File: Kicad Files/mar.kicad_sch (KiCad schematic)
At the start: 21 parts

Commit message: started tidy up in control
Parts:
- gave numbers to parts that had none: 21
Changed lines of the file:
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@@
   (symbol (lib_id "8bit-computer-rescue:LED_ALT-Device") (at 160.02 30.48 180) (unit 1)
     (in_bom yes) (on_board yes)
-    (property "Reference" "" (id 0) (at 160.02 33.02 0))
+    (property "Reference" "D96" (id 0) (at 160.02 33.02 0))
     (property "Value" "YELLOW" (id 1) (at 160.02 27.94 0))
     (property "Footprint" "LED_THT:LED_D5.0mm" (id 2) (at 160.02 30.48 0)
@@
   (symbol (lib_id "8bit-computer-rescue:LED_ALT-Device") (at 160.02 38.1 180) (unit 1)
     (in_bom yes) (on_board yes)
-    (property "Reference" "" (id 0) (at 160.02 40.64 0))
+    (property "Reference" "D97" (id 0) (at 160.02 40.64 0))
     (property "Value" "YELLOW" (id 1) (at 160.02 35.56 0))
     (property "Footprint" "LED_THT:LED_D5.0mm" (id 2) (at 160.02 38.1 0)
@@
   (symbol (lib_id "8bit-computer-rescue:LED_ALT-Device") (at 160.02 45.72 180) (unit 1)
     (in_bom yes) (on_board yes)
-    (property "Reference" "" (id 0) (at 160.02 48.26 0))
+    (property "Reference" "D98" (id 0) (at 160.02 48.26 0))
     (property "Value" "YELLOW" (id 1) (at 160.02 43.18 0))
     (property "Footprint" "LED_THT:LED_D5.0mm" (id 2) (at 160.02 45.72 0)
@@
   (symbol (lib_id "8bit-computer-rescue:LED_ALT-Device") (at 160.02 53.34 180) (unit 1)
     (in_bom yes) (on_board yes)
-    (property "Reference" "" (id 0) (at 160.02 55.88 0))
+    (property "Reference" "D99" (id 0) (at 160.02 55.88 0))
     (property "Value" "YELLOW" (id 1) (at 160.02 50.8 0))
     (property "Footprint" "LED_THT:LED_D5.0mm" (id 2) (at 160.02 53.34 0)
@@
   (symbol (lib_id "Device:R") (at 170.18 30.48 90) (unit 1)
     (in_bom yes) (on_board yes)
-    (property "Reference" "" (id 0) (at 170.18 28.448 90))
+    (property "Reference" "R126" (id 0) (at 170.18 28.448 90))
     (property "Value" "220" (id 1) (at 170.18 30.48 90))
     (property "Footprint" "Resistor_THT:R_Axial_DIN0207_L6.3mm_D2.5mm_P7.62mm_Horizontal" (id 2) (at 170.18 32.258 90)
@@
   (symbol (lib_id "Device:R") (at 170.18 38.1 90) (unit 1)
     (in_bom yes) (on_board yes)
-    (property "Reference" "" (id 0) (at 170.18 36.068 90))
+    (property "Reference" "R127" (id 0) (at 170.18 36.068 90))
     (property "Value" "220" (id 1) (at 170.18 38.1 90))
     (property "Footprint" "Resistor_THT:R_Axial_DIN0207_L6.3mm_D2.5mm_P7.62mm_Horizontal" (id 2) (at 170.18 39.878 90)
@@
   (symbol (lib_id "Device:R") (at 170.18 45.72 90) (unit 1)
     (in_bom yes) (on_board yes)
-    (property "Reference" "" (id 0) (at 170.18 43.688 90))
+    (property "Reference" "R128" (id 0) (at 170.18 43.688 90))
     (property "Value" "220" (id 1) (at 170.18 45.72 90))
     (property "Footprint" "Resistor_THT:R_Axial_DIN0207_L6.3mm_D2.5mm_P7.62mm_Horizontal" (id 2) (at 170.18 47.498 90)
@@
   (symbol (lib_id "Device:R") (at 170.18 53.34 90) (unit 1)
     (in_bom yes) (on_board yes)
-    (property "Reference" "" (id 0) (at 170.18 51.308 90))
+    (property "Reference" "R129" (id 0) (at 170.18 51.308 90))
     (property "Value" "220" (id 1) (at 170.18 53.34 90))
     (property "Footprint" "Resistor_THT:R_Axial_DIN0207_L6.3mm_D2.5mm_P7.62mm_Horizontal" (id 2) (at 170.18 55.118 90)
@@
   (symbol (lib_id "Device:C") (at 171.45 140.97 0) (unit 1)
     (in_bom yes) (on_board yes)
-    (property "Reference" "" (id 0) (at 172.085 138.43 0)
+    (property "Reference" "C16" (id 0) (at 172.085 138.43 0)
       (effects (font (size 1.27 1.27)) (justify left))
     )
@@
   (symbol (lib_id "74xx:74LS157") (at 144.78 107.95 90) (unit 1)
     (in_bom yes) (on_board yes)
-    (property "Reference" "" (id 0) (at 171.2976 106.7816 90)
+    (property "Reference" "U57" (id 0) (at 171.2976 106.7816 90)
       (effects (font (size 1.27 1.27)) (justify right))
     )
@@
   (symbol (lib_id "74xx:74LS157") (at 68.58 107.95 90) (unit 1)
     (in_bom yes) (on_board yes)
-    (property "Reference" "" (id 0) (at 95.0976 106.7816 90)
+    (property "Reference" "U56" (id 0) (at 95.0976 106.7816 90)
       (effects (font (size 1.27 1.27)) (justify right))
     )
@@
   (symbol (lib_id "74xx:74LS173") (at 144.78 168.91 90) (unit 1)
     (in_bom yes) (on_board yes)
-    (property "Reference" "" (id 0) (at 168.7576 167.7416 90)
+    (property "Reference" "U59" (id 0) (at 168.7576 167.7416 90)
       (effects (font (size 1.27 1.27)) (justify right))
     )
@@
   (symbol (lib_id "74xx:74LS173") (at 68.58 168.91 90) (unit 1)
     (in_bom yes) (on_board yes)
-    (property "Reference" "" (id 0) (at 92.5576 167.7416 90)
+    (property "Reference" "U58" (id 0) (at 92.5576 167.7416 90)
       (effects (font (size 1.27 1.27)) (justify right))
     )
@@
   (symbol (lib_id "8bit-computer-rescue:LED_ALT-Device") (at 160.02 60.96 180) (unit 1)
     (in_bom yes) (on_board yes)
-    (property "Reference" "" (id 0) (at 160.02 63.5 0))
+    (property "Reference" "D100" (id 0) (at 160.02 63.5 0))
     (property "Value" "YELLOW" (id 1) (at 160.02 58.42 0))
     (property "Footprint" "LED_THT:LED_D5.0mm" (id 2) (at 160.02 60.96 0)
@@
   (symbol (lib_id "8bit-computer-rescue:LED_ALT-Device") (at 160.02 68.58 180) (unit 1)
     (in_bom yes) (on_board yes)
-    (property "Reference" "" (id 0) (at 160.02 71.12 0))
+    (property "Reference" "D101" (id 0) (at 160.02 71.12 0))
     (property "Value" "YELLOW" (id 1) (at 160.02 66.04 0))
     (property "Footprint" "LED_THT:LED_D5.0mm" (id 2) (at 160.02 68.58 0)
@@
   (symbol (lib_id "8bit-computer-rescue:LED_ALT-Device") (at 160.02 76.2 180) (unit 1)
     (in_bom yes) (on_board yes)
-    (property "Reference" "" (id 0) (at 160.02 78.74 0))
+    (property "Reference" "D102" (id 0) (at 160.02 78.74 0))
     (property "Value" "YELLOW" (id 1) (at 160.02 73.66 0))
     (property "Footprint" "LED_THT:LED_D5.0mm" (id 2) (at 160.02 76.2 0)
@@
   (symbol (lib_id "8bit-computer-rescue:LED_ALT-Device") (at 160.02 83.82 180) (unit 1)
     (in_bom yes) (on_board yes)
-    (property "Reference" "" (id 0) (at 160.02 86.36 0))
+    (property "Reference" "D103" (id 0) (at 160.02 86.36 0))
     (property "Value" "YELLOW" (id 1) (at 160.02 81.28 0))
     (property "Footprint" "LED_THT:LED_D5.0mm" (id 2) (at 160.02 83.82 0)
@@
   (symbol (lib_id "Device:R") (at 170.18 60.96 90) (unit 1)
     (in_bom yes) (on_board yes)
-    (property "Reference" "" (id 0) (at 170.18 58.928 90))
+    (property "Reference" "R130" (id 0) (at 170.18 58.928 90))
     (property "Value" "220" (id 1) (at 170.18 60.96 90))
     (property "Footprint" "Resistor_THT:R_Axial_DIN0207_L6.3mm_D2.5mm_P7.62mm_Horizontal" (id 2) (at 170.18 62.738 90)
@@
   (symbol (lib_id "Device:R") (at 170.18 68.58 90) (unit 1)
     (in_bom yes) (on_board yes)
-    (property "Reference" "" (id 0) (at 170.18 66.548 90))
+    (property "Reference" "R131" (id 0) (at 170.18 66.548 90))
     (property "Value" "220" (id 1) (at 170.18 68.58 90))
     (property "Footprint" "Resistor_THT:R_Axial_DIN0207_L6.3mm_D2.5mm_P7.62mm_Horizontal" (id 2) (at 170.18 70.358 90)
@@
   (symbol (lib_id "Device:R") (at 170.18 76.2 90) (unit 1)
     (in_bom yes) (on_board yes)
-    (property "Reference" "" (id 0) (at 170.18 74.168 90))
+    (property "Reference" "R132" (id 0) (at 170.18 74.168 90))
     (property "Value" "220" (id 1) (at 170.18 76.2 90))
     (property "Footprint" "Resistor_THT:R_Axial_DIN0207_L6.3mm_D2.5mm_P7.62mm_Horizontal" (id 2) (at 170.18 77.978 90)
@@
   (symbol (lib_id "Device:R") (at 170.18 83.82 90) (unit 1)
     (in_bom yes) (on_board yes)
-    (property "Reference" "" (id 0) (at 170.18 81.788 90))
+    (property "Reference" "R133" (id 0) (at 170.18 81.788 90))
     (property "Value" "220" (id 1) (at 170.18 83.82 90))
     (property "Footprint" "Resistor_THT:R_Axial_DIN0207_L6.3mm_D2.5mm_P7.62mm_Horizontal" (id 2) (at 170.18 85.598 90)

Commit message: work on cl
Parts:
- C10: renamed from C16; value 0.1µF -> C
- R46: renamed from R126; value 220 -> R
- R47: renamed from R127; value 220 -> R
- R48: renamed from R128; value 220 -> R
- R49: renamed from R129; value 220 -> R
- R50: renamed from R130; value 220 -> R
- R51: renamed from R131; value 220 -> R
- R52: renamed from R132; value 220 -> R
- R53: renamed from R133; value 220 -> R
- renumbered D96 to D16, D97 to D17, D98 to D18, D99 to D19, D100 to D20, D101 to D21, D102 to D22, D103 to D23, U56 to U13, U58 to U14, U57 to U15, U59 to U16

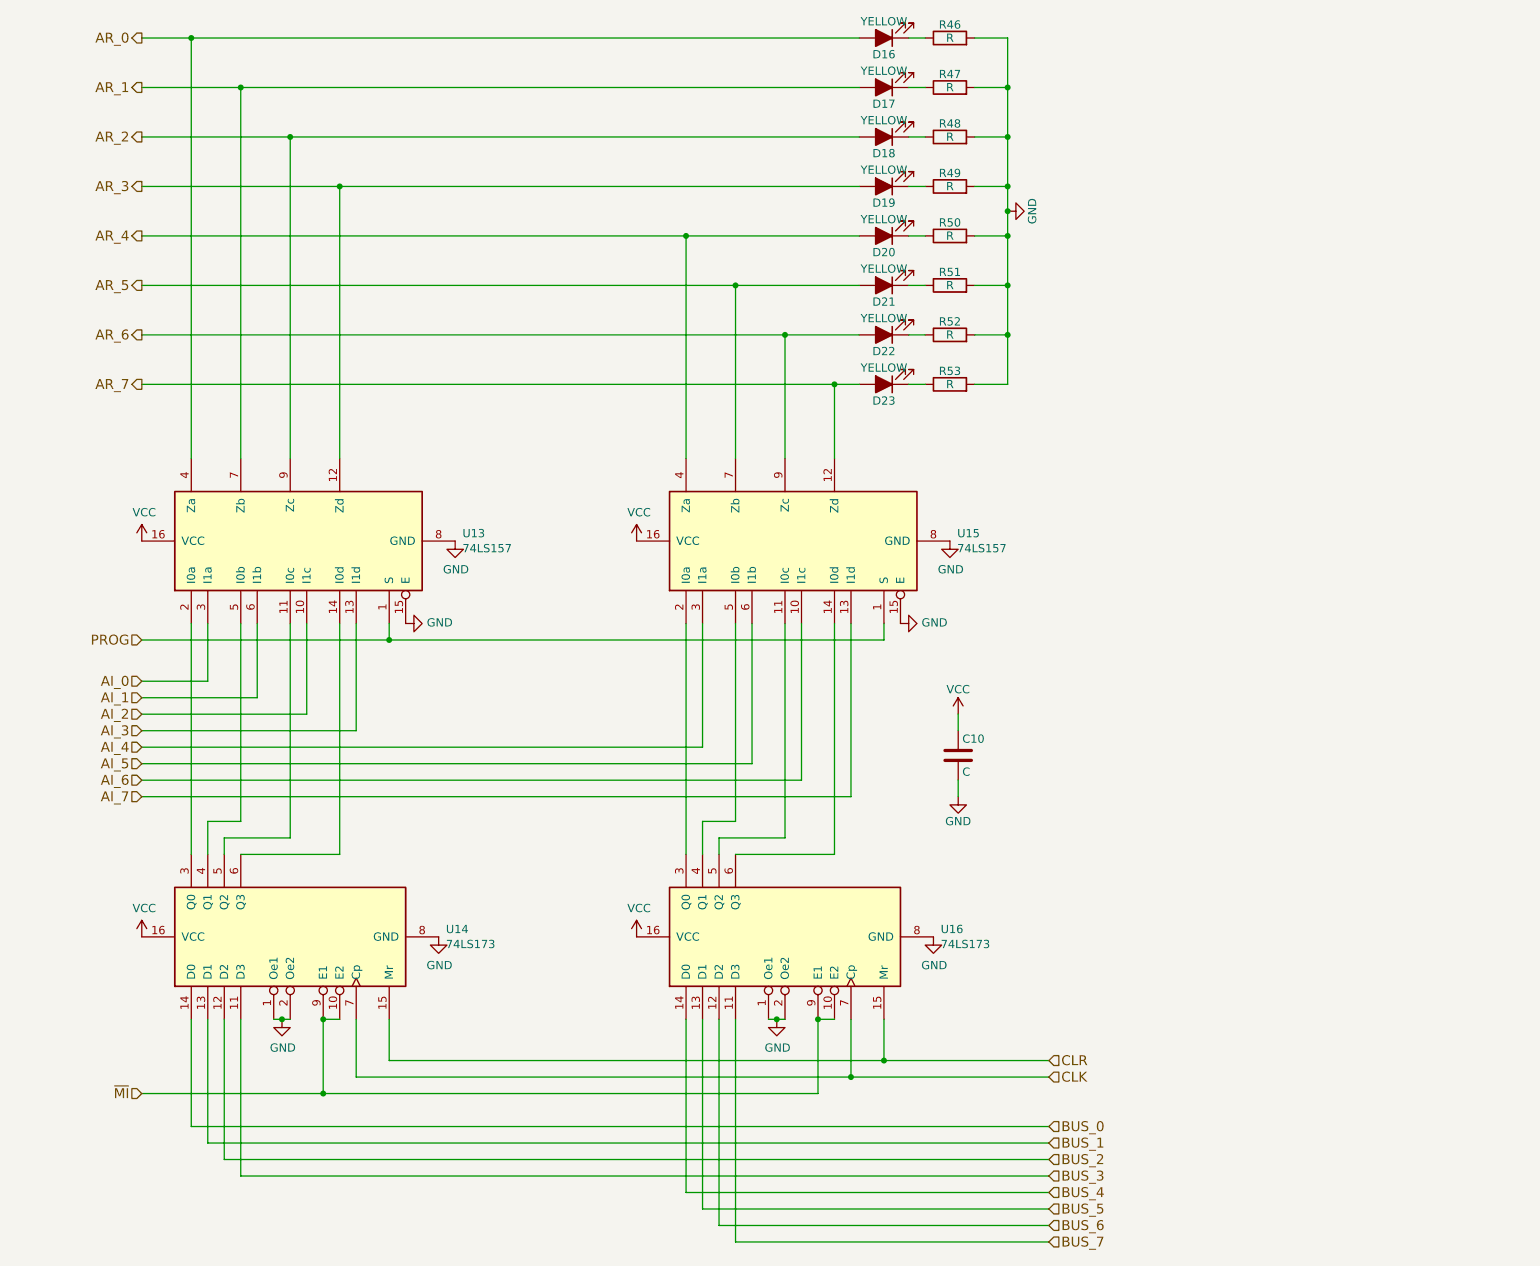
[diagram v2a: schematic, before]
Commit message: changed to 16bit Addr Bus
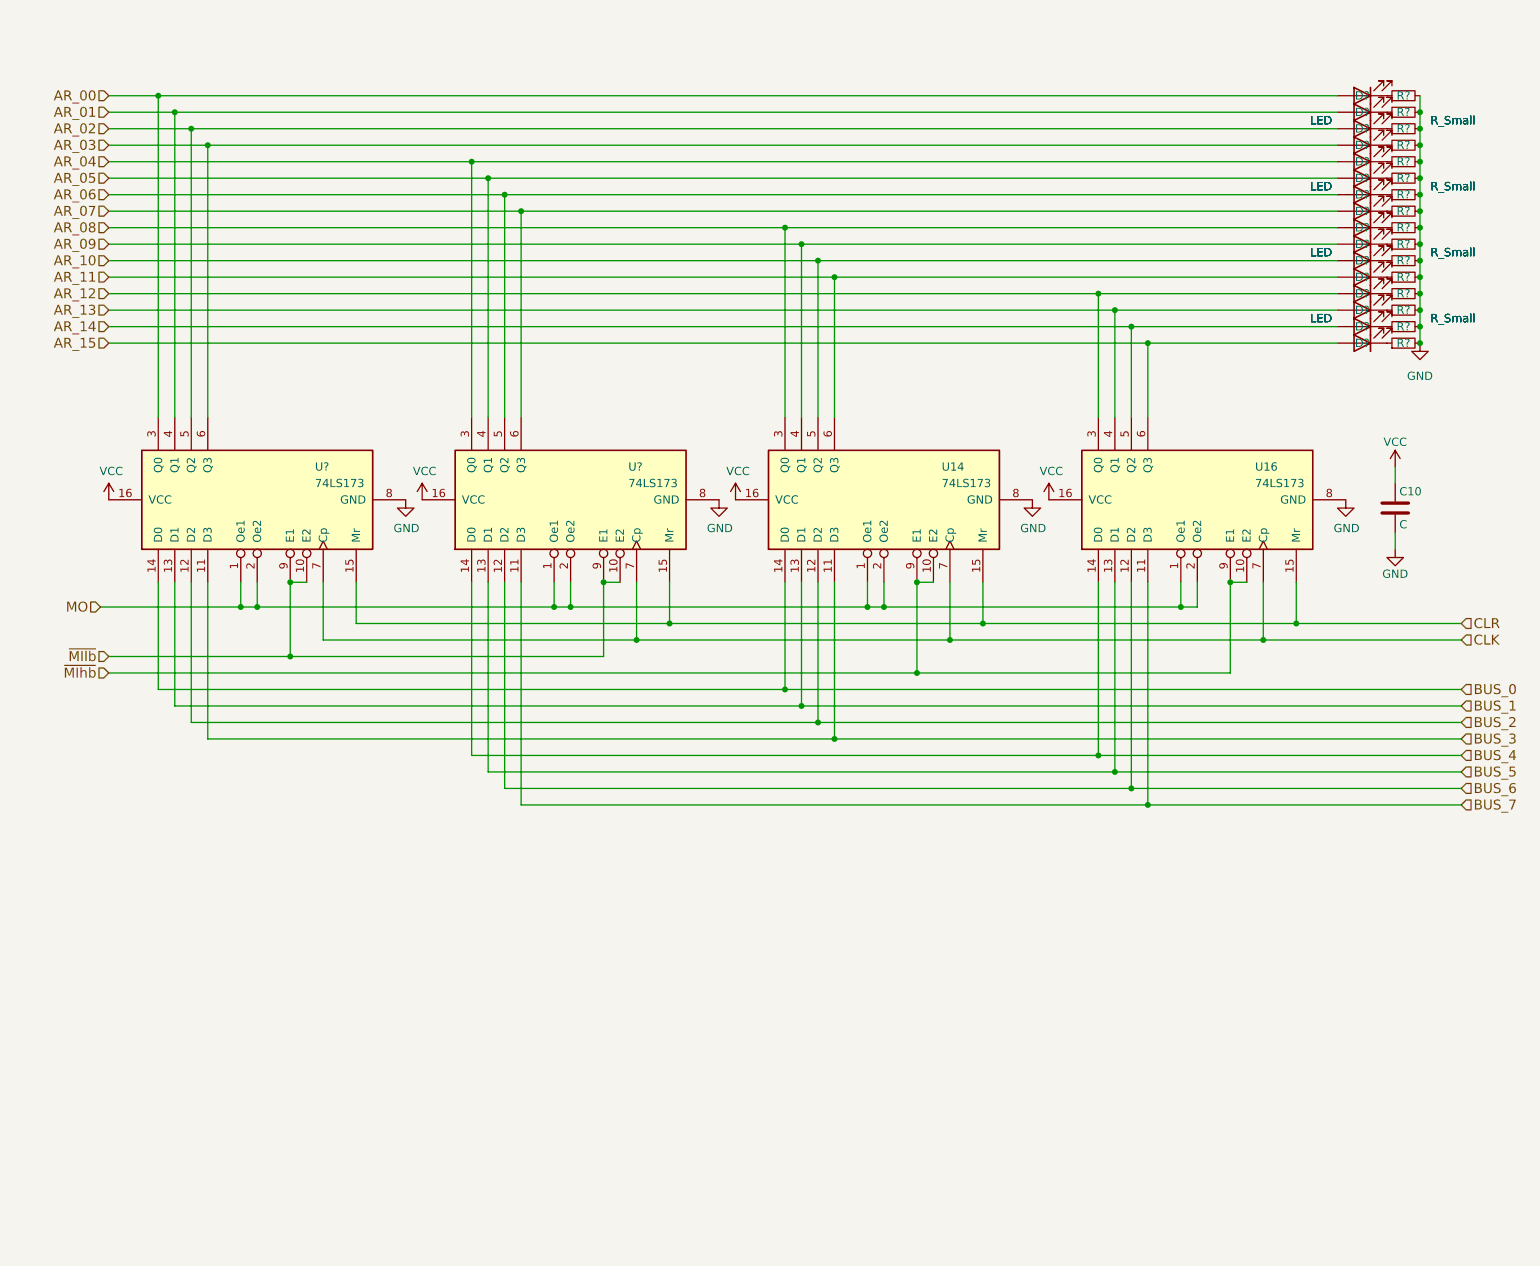
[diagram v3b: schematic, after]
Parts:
- removed D16, D17, D18, D19, D20, D21, D22, D23: YELLOW, LED_THT:LED_D5.0mm, symbol 8bit-computer-rescue:LED_ALT-Device
- removed R46, R47, R48, R49, R50, R51, R52, R53: R, Resistor_THT:R_Axial_DIN0207_L6.3mm_D2.5mm_P7.62mm_Horizontal, symbol Device:R
- removed U13, U15: 74LS157, symbol 74xx:74LS157
- added D? (x16): LED, symbol Device:LED
- added R? (x16): R_Small, symbol Device:R_Small
- added U? (x2): 74LS173, symbol 74xx:74LS173
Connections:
- net BUS_0: now also U?.14 (D0)
- net BUS_1: now also U?.13 (D1)
- net BUS_2: now also U?.12 (D2)
- net BUS_3: now also U?.11 (D3)
- net BUS_4: now also U?.14 (D0)
- net BUS_5: now also U?.13 (D1)
- net BUS_6: now also U?.12 (D2)
- net BUS_7: now also U?.11 (D3)
- net CLK: now also U?.7 (Cp), U?.7 (Cp)
- net CLR: now also U?.15 (Mr), U?.15 (Mr)
- net GND: now also R?.2, R?.2, R?.2, R?.2, R?.2, R?.2, R?.2, R?.2, R?.2, R?.2, R?.2, R?.2, R?.2, R?.2, R?.2, R?.2, U?.8 (GND), U?.8 (GND); no longer U14.1 (Oe1), U14.2 (Oe2), U16.1 (Oe1), U16.2 (Oe2)
- net VCC: now also U?.16 (VCC), U?.16 (VCC)
- net AR_14: now reaches U16.5 (Q2)
- net AR_14: now also D?.2 (A)
- net AR_15: now reaches U16.6 (Q3)
- net AR_15: now also D?.2 (A)
- net AR_12: now reaches U16.3 (Q0)
- net AR_12: now also D?.2 (A)
- net AR_13: now reaches U16.4 (Q1)
- net AR_13: now also D?.2 (A)
- net AR_10: now reaches U14.5 (Q2)
- net AR_10: now also D?.2 (A)
- net AR_11: now reaches U14.6 (Q3)
- net AR_11: now also D?.2 (A)
- net AR_08: now reaches U14.3 (Q0)
- net AR_08: now also D?.2 (A)
- net AR_09: now reaches U14.4 (Q1)
- net AR_09: now also D?.2 (A)
- net ~{MI} renamed ~{MIhb}
- new net: D?.1 (K), R?.1 (x16)
- new net AR_00: D?.2 (A), U?.3 (Q0)
- new net AR_01: D?.2 (A), U?.4 (Q1)
- new net AR_02: D?.2 (A), U?.5 (Q2)
- new net AR_03: D?.2 (A), U?.6 (Q3)
- new net AR_04: D?.2 (A), U?.3 (Q0)
- new net AR_05: D?.2 (A), U?.4 (Q1)
- new net AR_06: D?.2 (A), U?.5 (Q2)
- new net AR_07: D?.2 (A), U?.6 (Q3)
- new net MO: U14.1 (Oe1), U14.2 (Oe2), U16.1 (Oe1), U16.2 (Oe2), U?.1 (Oe1), U?.1 (Oe1), U?.2 (Oe2), U?.2 (Oe2)
- new net ~{MIlb}: U?.10 (E2), U?.10 (E2), U?.9 (E1), U?.9 (E1)
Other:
- moved on the sheet: C10, U14, U16

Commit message: w1
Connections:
- net AR_00 renamed ABUS_00
- net AR_01 renamed ABUS_01
- net AR_02 renamed ABUS_02
- net AR_03 renamed ABUS_03
- net AR_04 renamed ABUS_04
- net AR_05 renamed ABUS_05
- net AR_06 renamed ABUS_06
- net AR_07 renamed ABUS_07
- net AR_08 renamed ABUS_08
- net AR_09 renamed ABUS_09
- net AR_10 renamed ABUS_10
- net AR_11 renamed ABUS_11
- net AR_12 renamed ABUS_12
- net AR_13 renamed ABUS_13
- net AR_14 renamed ABUS_14
- net AR_15 renamed ABUS_15
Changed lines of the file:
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@@
     (effects (font (size 1.524 1.524)) (justify left))
   )
-  (hierarchical_label "AR_08" (shape input) (at 40.64 59.69 180)
+  (hierarchical_label "ABUS_08" (shape tri_state) (at 40.64 59.69 180)
     (effects (font (size 1.524 1.524)) (justify right))
   )
-  (hierarchical_label "AR_05" (shape input) (at 40.64 52.07 180)
+  (hierarchical_label "ABUS_05" (shape tri_state) (at 40.64 52.07 180)
     (effects (font (size 1.524 1.524)) (justify right))
   )
-  (hierarchical_label "AR_02" (shape input) (at 40.64 44.45 180)
+  (hierarchical_label "ABUS_02" (shape tri_state) (at 40.64 44.45 180)
     (effects (font (size 1.524 1.524)) (justify right))
   )
@@
     (effects (font (size 1.524 1.524)) (justify right))
   )
-  (hierarchical_label "AR_11" (shape input) (at 40.64 67.31 180)
+  (hierarchical_label "ABUS_11" (shape tri_state) (at 40.64 67.31 180)
     (effects (font (size 1.524 1.524)) (justify right))
   )
@@
     (effects (font (size 1.524 1.524)) (justify right))
   )
-  (hierarchical_label "AR_07" (shape input) (at 40.64 57.15 180)
+  (hierarchical_label "ABUS_07" (shape tri_state) (at 40.64 57.15 180)
     (effects (font (size 1.524 1.524)) (justify right))
   )
-  (hierarchical_label "AR_14" (shape input) (at 40.64 74.93 180)
+  (hierarchical_label "ABUS_14" (shape tri_state) (at 40.64 74.93 180)
     (effects (font (size 1.524 1.524)) (justify right))
   )
@@
     (effects (font (size 1.524 1.524)) (justify left))
   )
-  (hierarchical_label "AR_06" (shape input) (at 40.64 54.61 180)
+  (hierarchical_label "ABUS_06" (shape tri_state) (at 40.64 54.61 180)
     (effects (font (size 1.524 1.524)) (justify right))
   )
@@
     (effects (font (size 1.524 1.524)) (justify left))
   )
-  (hierarchical_label "AR_09" (shape input) (at 40.64 62.23 180)
+  (hierarchical_label "ABUS_09" (shape tri_state) (at 40.64 62.23 180)
     (effects (font (size 1.524 1.524)) (justify right))
   )
@@
     (effects (font (size 1.524 1.524)) (justify left))
   )
-  (hierarchical_label "AR_04" (shape input) (at 40.64 49.53 180)
+  (hierarchical_label "ABUS_04" (shape tri_state) (at 40.64 49.53 180)
     (effects (font (size 1.524 1.524)) (justify right))
   )
@@
     (effects (font (size 1.524 1.524)) (justify left))
   )
-  (hierarchical_label "AR_03" (shape input) (at 40.64 46.99 180)
+  (hierarchical_label "ABUS_03" (shape tri_state) (at 40.64 46.99 180)
     (effects (font (size 1.524 1.524)) (justify right))
   )
-  (hierarchical_label "AR_00" (shape input) (at 40.64 39.37 180)
+  (hierarchical_label "ABUS_00" (shape tri_state) (at 40.64 39.37 180)
     (effects (font (size 1.524 1.524)) (justify right))
   )
@@
     (effects (font (size 1.524 1.524)) (justify right))
   )
-  (hierarchical_label "AR_12" (shape input) (at 40.64 69.85 180)
+  (hierarchical_label "ABUS_12" (shape tri_state) (at 40.64 69.85 180)
     (effects (font (size 1.524 1.524)) (justify right))
   )
-  (hierarchical_label "AR_15" (shape input) (at 40.64 77.47 180)
+  (hierarchical_label "ABUS_15" (shape tri_state) (at 40.64 77.47 180)
     (effects (font (size 1.524 1.524)) (justify right))
   )
-  (hierarchical_label "AR_10" (shape input) (at 40.64 64.77 180)
+  (hierarchical_label "ABUS_10" (shape tri_state) (at 40.64 64.77 180)
     (effects (font (size 1.524 1.524)) (justify right))
   )
-  (hierarchical_label "AR_13" (shape input) (at 40.64 72.39 180)
+  (hierarchical_label "ABUS_13" (shape tri_state) (at 40.64 72.39 180)
     (effects (font (size 1.524 1.524)) (justify right))
   )
-  (hierarchical_label "AR_01" (shape input) (at 40.64 41.91 180)
+  (hierarchical_label "ABUS_01" (shape tri_state) (at 40.64 41.91 180)
     (effects (font (size 1.524 1.524)) (justify right))
   )

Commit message: work on pc2
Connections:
- net MO renamed ~{MO}
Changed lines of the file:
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@@
     (effects (font (size 1.524 1.524)) (justify right))
   )
-  (hierarchical_label "MO" (shape input) (at 39.37 118.11 180)
+  (hierarchical_label "~{MO}" (shape input) (at 39.37 118.11 180)
     (effects (font (size 1.524 1.524)) (justify right))
   )
